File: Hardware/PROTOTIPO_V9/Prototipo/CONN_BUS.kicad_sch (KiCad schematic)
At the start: 2 parts, among them J4 Conn_01x10, J5 Conn_01x10

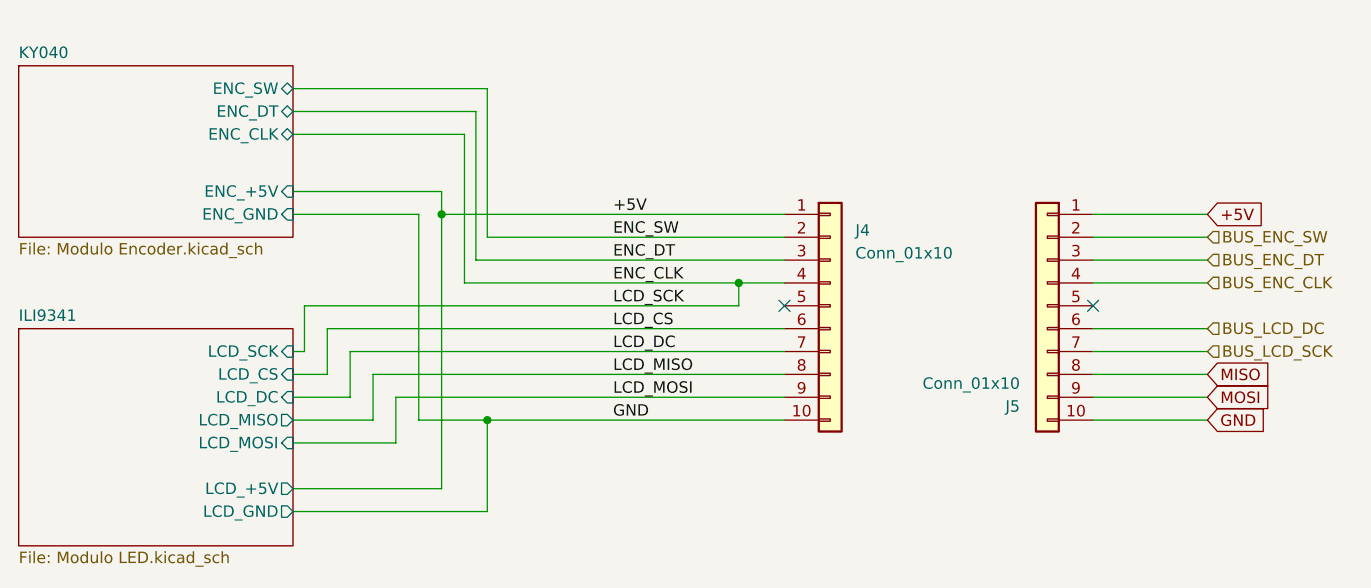
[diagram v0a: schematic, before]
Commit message: sch ILI9341 y sch ADS1115
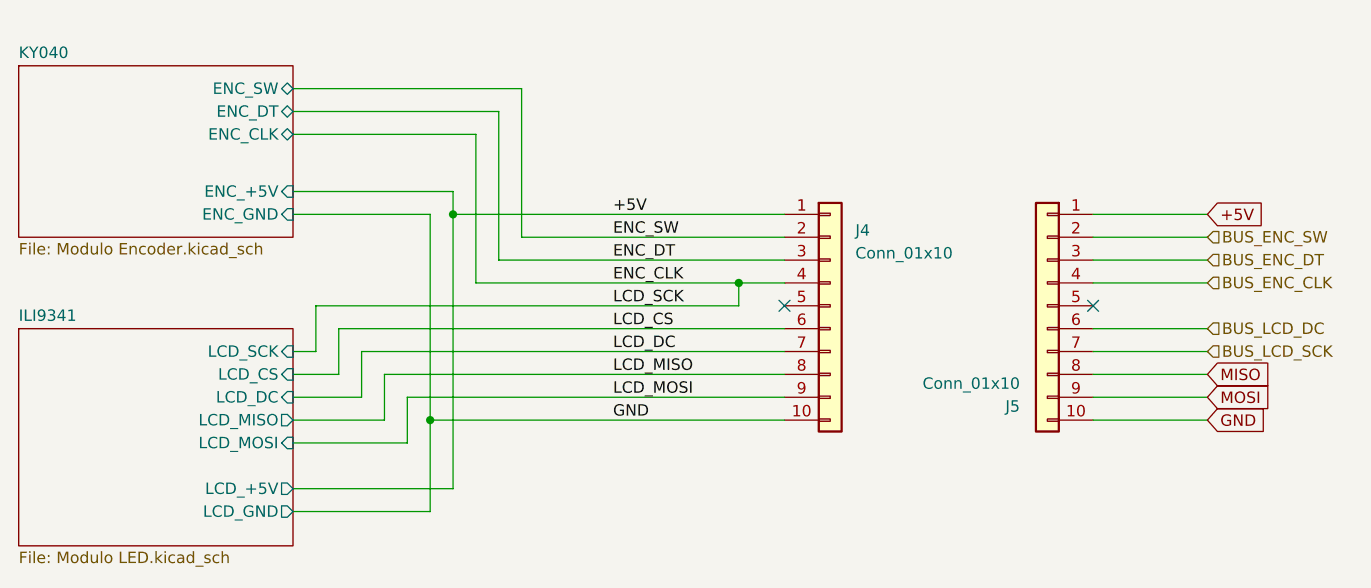
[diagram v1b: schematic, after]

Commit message: ERC: 0 errores
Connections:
- net BUS_LCD_SCK is gone; now on net BUS_LCD_DC: J5.7 (Pin_7)
- net BUS_LCD_DC: no longer J5.6 (Pin_6)
- new net BUS_LCD_CS: J5.6 (Pin_6)
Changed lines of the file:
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@@
 		)
 	)
-	(hierarchical_label "BUS_LCD_DC"
+	(hierarchical_label "BUS_LCD_CS"
 		(shape input)
 		(at 236.22 71.12 0)
@@
 		)
 	)
-	(hierarchical_label "BUS_LCD_SCK"
+	(hierarchical_label "BUS_LCD_DC"
 		(shape input)
 		(at 236.22 73.66 0)

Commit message: Asignación de huellas
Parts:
- J4, J5: footprint (none) -> Connector_PinSocket_2.54mm:PinSocket_2x05_P2.54mm_Vertical
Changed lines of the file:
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@@
 			)
 		)
-		(property "Footprint" ""
+		(property "Footprint" "Connector_PinSocket_2.54mm:PinSocket_2x05_P2.54mm_Vertical"
 			(at 194.31 68.58 0)
 			(effects
@@
 			)
 		)
-		(property "Footprint" ""
+		(property "Footprint" "Connector_PinSocket_2.54mm:PinSocket_2x05_P2.54mm_Vertical"
 			(at 218.44 68.58 0)
 			(effects

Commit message: Ruteo de PCB Superior
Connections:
- net ENC_CLK is gone; now on net ENC_DT: J4.4 (Pin_4)
- net +5V: now also J4.8 (Pin_8), J5.8 (Pin_8); no longer J4.1 (Pin_1), J5.1 (Pin_1)
- net BUS_ENC_CLK: now also J5.2 (Pin_2); no longer J5.4 (Pin_4)
- net BUS_ENC_DT: now also J5.4 (Pin_4); no longer J5.3 (Pin_3)
- net BUS_ENC_SW: now also J5.6 (Pin_6); no longer J5.2 (Pin_2)
- net BUS_LCD_CS: now also J5.9 (Pin_9); no longer J5.6 (Pin_6)
- net ENC_DT: no longer J4.3 (Pin_3)
- net ENC_SW: now also J4.6 (Pin_6); no longer J4.2 (Pin_2)
- net LCD_CS: now also J4.9 (Pin_9); no longer J4.6 (Pin_6)
- net LCD_MISO: now also J4.3 (Pin_3); no longer J4.8 (Pin_8)
- net LCD_MOSI: now also J4.5 (Pin_5); no longer J4.9 (Pin_9)
- net MISO: now also J5.3 (Pin_3); no longer J5.8 (Pin_8)
- net MOSI: now also J5.5 (Pin_5); no longer J5.9 (Pin_9)
- new net CLK: J4.2 (Pin_2)
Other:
- moved on the sheet: J4

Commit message: Migración de sch a BlackPill
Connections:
- net LCD_SCK: now reaches J4.1 (Pin_1)
- net BUS_LCD_SCK: now reaches J5.1 (Pin_1)
- net CLK renamed ENC_CLK
- no-connect marks 2 -> 0
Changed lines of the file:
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@@
 	(paper "A4")
+	(junction
+		(at 149.86 81.28)
+		(diameter 0)
+		(color 0 0 0 0)
+	)
 	(junction
 		(at 152.4 76.2)
@@
 		(color 0 0 0 0)
 	)
-	(junction
-		(at 149.86 81.28)
-		(diameter 0)
-		(color 0 0 0 0)
-	)
-	(junction
-		(at 160.02 60.96)
-		(diameter 0)
-		(color 0 0 0 0)
-	)
-	(no_connect
-		(at 223.52 58.42)
-	)
-	(no_connect
-		(at 193.04 58.42)
-	)
 	(wire
 		(pts
@@
 	(wire
 		(pts
-			(xy 134.62 55.88) (xy 152.4 55.88)
-		)
-		(stroke
-			(width 0)
-			(type default)
-		)
-	)
-	(wire
-		(pts
-			(xy 134.62 58.42) (xy 149.86 58.42)
+			(xy 134.62 53.34) (xy 152.4 53.34)
+		)
+		(stroke
+			(width 0)
+			(type default)
+		)
+	)
+	(wire
+		(pts
+			(xy 134.62 55.88) (xy 149.86 55.88)
 		)
 		(stroke
@@
 	(wire
 		(pts
-			(xy 137.16 60.96) (xy 160.02 60.96)
-		)
-		(stroke
-			(width 0)
-			(type default)
-		)
-	)
-	(wire
-		(pts
-			(xy 137.16 60.96) (xy 137.16 73.66)
-		)
-		(stroke
-			(width 0)
-			(type default)
-		)
-	)
-	(wire
-		(pts
-			(xy 149.86 58.42) (xy 149.86 81.28)
+			(xy 137.16 58.42) (xy 137.16 73.66)
+		)
+		(stroke
+			(width 0)
+			(type default)
+		)
+	)
+	(wire
+		(pts
+			(xy 149.86 55.88) (xy 149.86 81.28)
 		)
 		(stroke
@@
 	(wire
 		(pts
+			(xy 160.02 60.96) (xy 193.04 60.96)
+		)
+		(stroke
+			(width 0)
+			(type default)
+		)
+	)
+	(wire
+		(pts
 			(xy 223.52 78.74) (xy 236.22 78.74)
 		)
@@
 	(wire
 		(pts
-			(xy 152.4 55.88) (xy 152.4 76.2)
-		)
-		(stroke
-			(width 0)
-			(type default)
-		)
-	)
-	(wire
-		(pts
-			(xy 134.62 49.53) (xy 154.94 49.53)
+			(xy 152.4 53.34) (xy 152.4 76.2)
+		)
+		(stroke
+			(width 0)
+			(type default)
+		)
+	)
+	(wire
+		(pts
+			(xy 134.62 46.99) (xy 154.94 46.99)
 		)
 		(stroke
@@
 	(wire
 		(pts
+			(xy 134.62 88.9) (xy 152.4 88.9)
+		)
+		(stroke
+			(width 0)
+			(type default)
+		)
+	)
+	(wire
+		(pts
+			(xy 223.52 58.42) (xy 236.22 58.42)
+		)
+		(stroke
+			(width 0)
+			(type default)
+		)
+	)
+	(wire
+		(pts
+			(xy 160.02 41.91) (xy 160.02 60.96)
+		)
+		(stroke
+			(width 0)
+			(type default)
+		)
+	)
+	(wire
+		(pts
+			(xy 139.7 63.5) (xy 193.04 63.5)
+		)
+		(stroke
+			(width 0)
+			(type default)
+		)
+	)
+	(wire
+		(pts
+			(xy 134.62 41.91) (xy 160.02 41.91)
+		)
+		(stroke
+			(width 0)
+			(type default)
+		)
+	)
+	(wire
+		(pts
+			(xy 147.32 83.82) (xy 147.32 78.74)
+		)
+		(stroke
+			(width 0)
+			(type default)
+		)
+	)
+	(wire
+		(pts
+			(xy 152.4 76.2) (xy 193.04 76.2)
+		)
+		(stroke
+			(width 0)
+			(type default)
+		)
+	)
+	(wire
+		(pts
+			(xy 134.62 78.74) (xy 142.24 78.74)
+		)
+		(stroke
+			(width 0)
+			(type default)
+		)
+	)
+	(wire
+		(pts
+			(xy 134.62 44.45) (xy 157.48 44.45)
+		)
+		(stroke
+			(width 0)
+			(type default)
+		)
+	)
+	(wire
+		(pts
+			(xy 134.62 91.44) (xy 149.86 91.44)
+		)
+		(stroke
+			(width 0)
+			(type default)
+		)
+	)
+	(wire
+		(pts
+			(xy 137.16 58.42) (xy 193.04 58.42)
+		)
+		(stroke
+			(width 0)
+			(type default)
+		)
+	)
+	(wire
+		(pts
 			(xy 152.4 76.2) (xy 152.4 88.9)
 		)
@@
 	(wire
 		(pts
-			(xy 160.02 44.45) (xy 160.02 60.96)
-		)
-		(stroke
-			(width 0)
-			(type default)
-		)
-	)
-	(wire
-		(pts
-			(xy 134.62 88.9) (xy 152.4 88.9)
-		)
-		(stroke
-			(width 0)
-			(type default)
-		)
-	)
-	(wire
-		(pts
-			(xy 139.7 63.5) (xy 193.04 63.5)
-		)
-		(stroke
-			(width 0)
-			(type default)
-		)
-	)
-	(wire
-		(pts
-			(xy 134.62 44.45) (xy 160.02 44.45)
-		)
-		(stroke
-			(width 0)
-			(type default)
-		)
-	)
-	(wire
-		(pts
-			(xy 147.32 83.82) (xy 147.32 78.74)
-		)
-		(stroke
-			(width 0)
-			(type default)
-		)
-	)
-	(wire
-		(pts
-			(xy 152.4 76.2) (xy 193.04 76.2)
-		)
-		(stroke
-			(width 0)
-			(type default)
-		)
-	)
-	(wire
-		(pts
-			(xy 134.62 78.74) (xy 142.24 78.74)
-		)
-		(stroke
-			(width 0)
-			(type default)
-		)
-	)
-	(wire
-		(pts
-			(xy 134.62 46.99) (xy 157.48 46.99)
-		)
-		(stroke
-			(width 0)
-			(type default)
-		)
-	)
-	(wire
-		(pts
-			(xy 134.62 91.44) (xy 149.86 91.44)
-		)
-		(stroke
-			(width 0)
-			(type default)
-		)
-	)
-	(wire
-		(pts
 			(xy 223.52 60.96) (xy 236.22 60.96)
 		)
@@
 	(wire
 		(pts
-			(xy 154.94 49.53) (xy 154.94 71.12)
+			(xy 154.94 46.99) (xy 154.94 71.12)
 		)
 		(stroke
@@
 	(wire
 		(pts
-			(xy 157.48 46.99) (xy 157.48 66.04)
+			(xy 157.48 44.45) (xy 157.48 66.04)
 		)
 		(stroke
@@
 		(pts
 			(xy 147.32 78.74) (xy 193.04 78.74)
-		)
-		(stroke
-			(width 0)
-			(type default)
-		)
-	)
-	(wire
-		(pts
-			(xy 160.02 60.96) (xy 193.04 60.96)
 		)
 		(stroke
@@
 		)
 	)
-	(label "CLK"
+	(label "ENC_CLK"
 		(at 172.72 60.96 0)
 		(effects
@@
 	(label "LCD_CS"
 		(at 172.72 78.74 0)
+		(effects
+			(font
+				(size 1.27 1.27)
+			)
+			(justify left bottom)
+		)
+	)
+	(label "LCD_SCK"
+		(at 172.72 58.42 0)
 		(effects
 			(font
@@
 		(shape input)
 		(at 236.22 73.66 0)
+		(effects
+			(font
+				(size 1.27 1.27)
+			)
+			(justify left)
+		)
+	)
+	(hierarchical_label "BUS_LCD_SCK"
+		(shape input)
+		(at 236.22 58.42 0)
 		(effects
 			(font
@@
 	)
 	(sheet
-		(at 104.14 41.91)
+		(at 104.14 39.37)
 		(size 30.48 19.05)
 		(exclude_from_sim no)
@@
 		)
 		(property "Sheetname" "KY040"
-			(at 104.14 41.1984 0)
+			(at 104.14 38.6584 0)
 			(effects
 				(font
@@
 		)
 		(property "Sheetfile" "Modulo Encoder.kicad_sch"
-			(at 104.14 61.5446 0)
+			(at 104.14 59.0046 0)
 			(effects
 				(font
@@
 		)
 		(pin "ENC_SW" bidirectional
-			(at 134.62 49.53 0)
+			(at 134.62 46.99 0)
 			(effects
 				(font
@@
 		)
 		(pin "ENC_DT" bidirectional
-			(at 134.62 46.99 0)
+			(at 134.62 44.45 0)
 			(effects
 				(font
@@
 		)
 		(pin "ENC_CLK" bidirectional
-			(at 134.62 44.45 0)
+			(at 134.62 41.91 0)
 			(effects
 				(font
@@
 		)
 		(pin "ENC_GND" input
-			(at 134.62 58.42 0)
+			(at 134.62 55.88 0)
 			(effects
 				(font
@@
 		)
 		(pin "ENC_+5V" input
-			(at 134.62 55.88 0)
-			(effects
-				(font
+			(at 134.62 53.34 0)
+			(effects
+				(font
